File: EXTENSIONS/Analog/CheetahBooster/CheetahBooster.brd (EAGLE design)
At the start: 83 x 73 mm, 31 parts

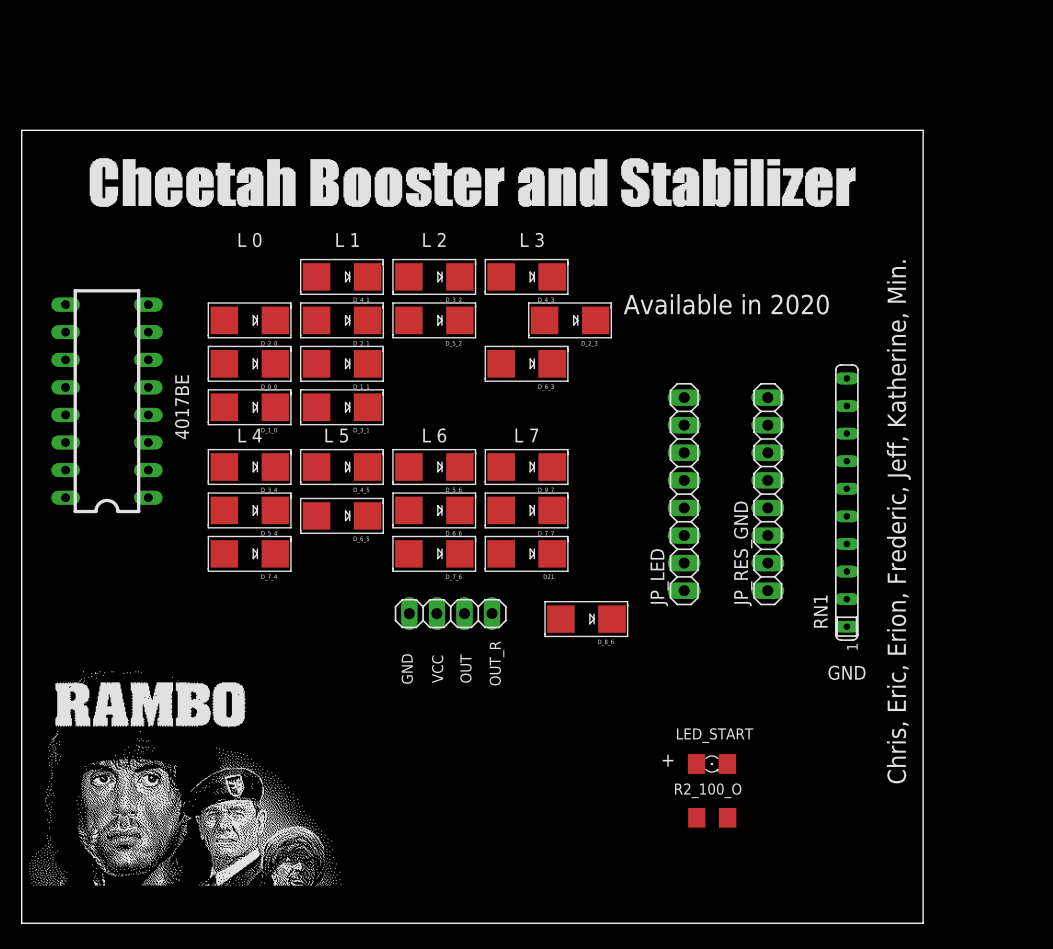
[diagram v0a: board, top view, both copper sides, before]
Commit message: Create CheetahBooster MCU
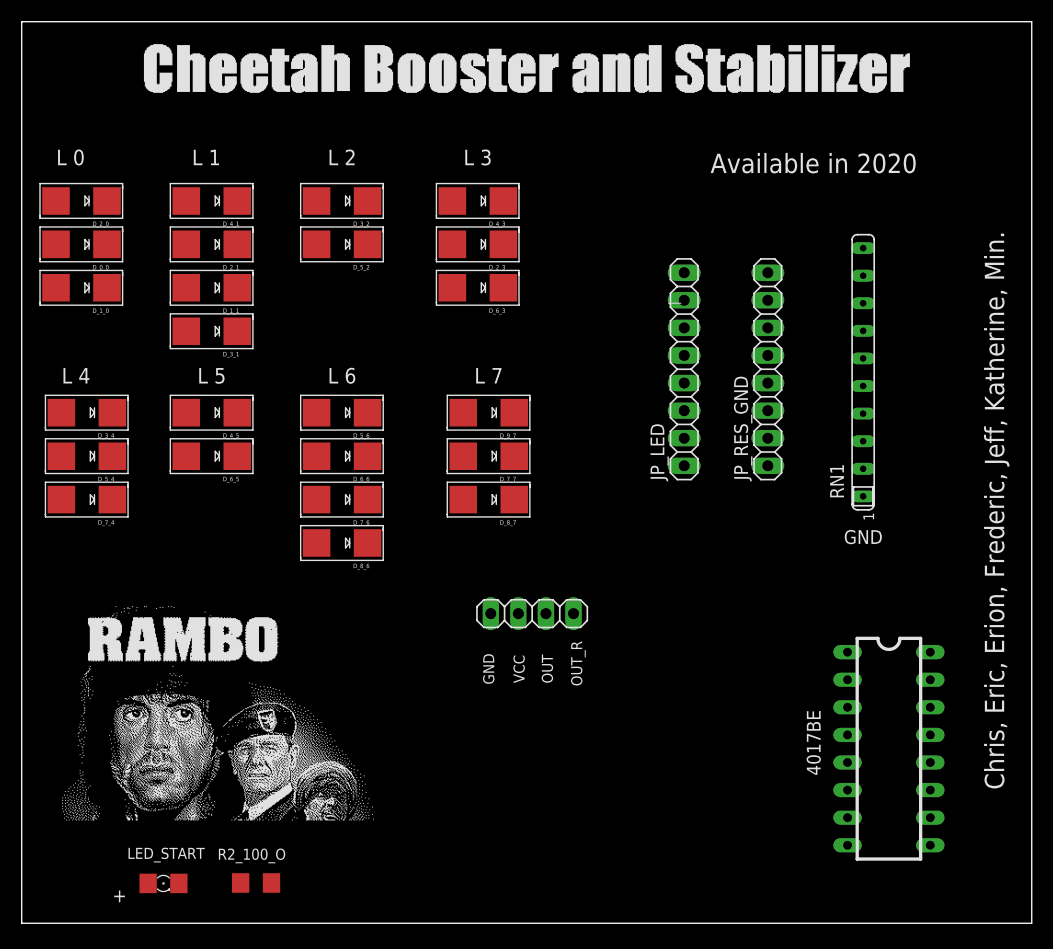
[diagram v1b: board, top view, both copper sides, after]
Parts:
- removed D21: (no value), adafruit:SMADIODE
- added D_8_7: (no value), adafruit:SMADIODE
- moved 4017BE 78.8 mm to (81.8, 28.1), turned to 270 degrees
- moved LED_START 51.7 mm to (15.1, 15.7)
- moved R2_100_O 42.4 mm to (23.6, 15.7)
- moved D_8_6 23.6 mm to (31.5, 47.0)
- moved D_0_0 19.0 mm to (7.50, 74.5)
- moved D_1_0 19.0 mm to (7.50, 70.5)
- moved D_2_0 19.0 mm to (7.50, 78.5)
- moved D_3_4 15.8 mm to (8.00, 59.0)
- moved D_5_4 15.8 mm to (8.00, 55.0)
- moved D_7_4 15.8 mm to (8.00, 51.0)
- moved D_1_1 13.9 mm to (19.5, 70.5)
- moved D_2_1 13.9 mm to (19.5, 74.5)
- moved D_3_1 13.9 mm to (19.5, 66.5)
- moved D_4_1 13.9 mm to (19.5, 78.5)
- moved D_6_5 13.2 mm to (19.5, 55.0)
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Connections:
- removed net D_8_7: D21.C
- removed net SEG_0_0: LED_START.A
- net LED_7: now also D_8_7.C
- net SEG_0: now also LED_START.A
- net SEG_8: now also D_8_7.A; no longer D21.A
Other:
- board size 83 x 73 mm -> 93 x 83 mm

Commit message: Create CheetahBooster MCU
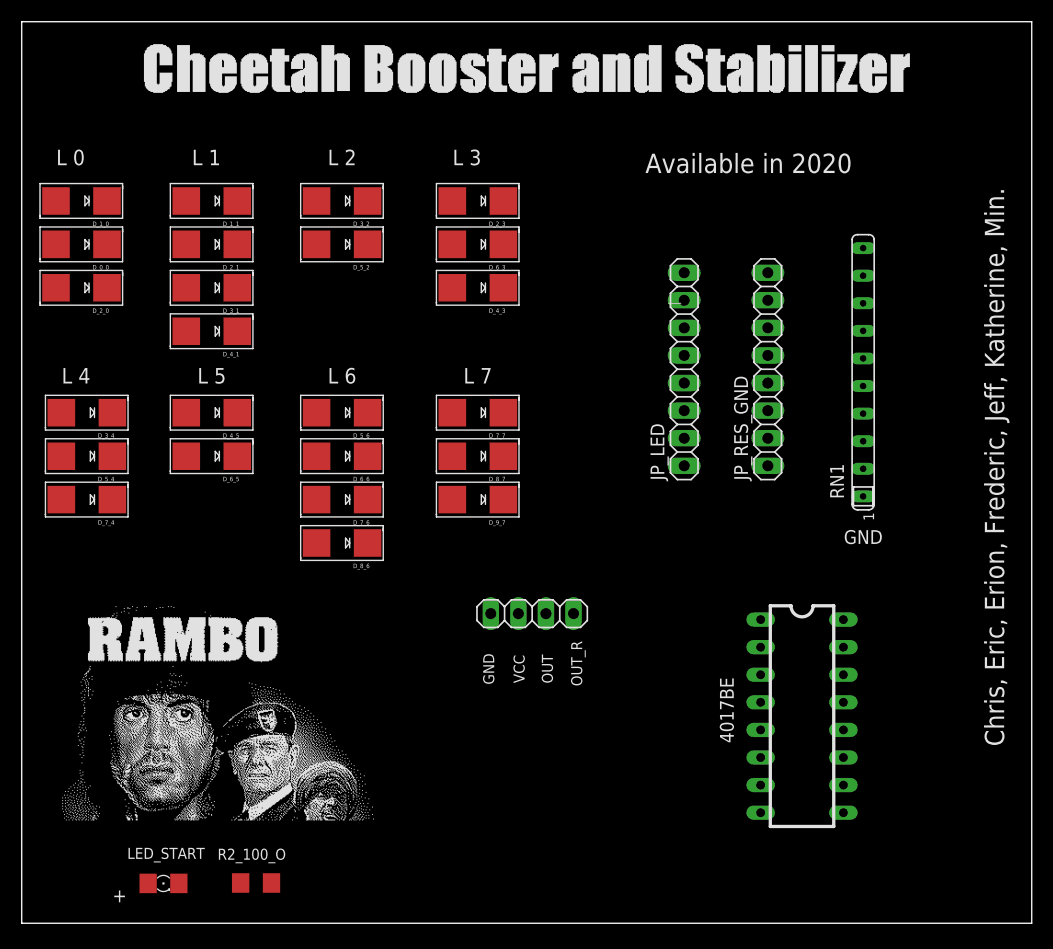
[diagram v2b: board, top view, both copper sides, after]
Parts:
- moved D_4_1 12.0 mm to (19.5, 66.5)
- moved 4017BE 8.54 mm to (73.8, 31.1)
- moved D_9_7 8.06 mm to (44.0, 51.0)
- moved D_1_0 8.00 mm to (7.50, 78.5)
- moved D_1_1 8.00 mm to (19.5, 78.5)
- moved D_2_0 8.00 mm to (7.50, 70.5)
- moved D_4_3 8.00 mm to (44.0, 70.5)
- moved D_7_7 4.12 mm to (44.0, 59.0)
- moved D_8_7 4.12 mm to (44.0, 55.0)
- moved D_2_3 4.00 mm to (44.0, 78.5)
- moved D_3_1 4.00 mm to (19.5, 70.5)
- moved D_6_3 4.00 mm to (44.0, 74.5)
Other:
- board text added: "CYCLE LED ================ 0 0 1 0, 1 2 0, 1, 3 3 1, 2, 4 4 1, 3, 5 5 2, 4, 6 6 3, 5, 6 7 4, 6, 7 8 6, 7 9 7"
- board text added: "PCBv2 - 2020.03"
- board text removed: "CYCLE/INSTRUCTION =============== LED 0 0,1,2,3 LED 1 1,2,4 LED 2 3,5 LED 3 2,4 LED 4 3,5,6 LED 5 4 LED 6 5,6,7 LED 7 6,7,8"
- board text removed: "PCBv1 - 2020.02"

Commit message: Create CheetahBooster MCU
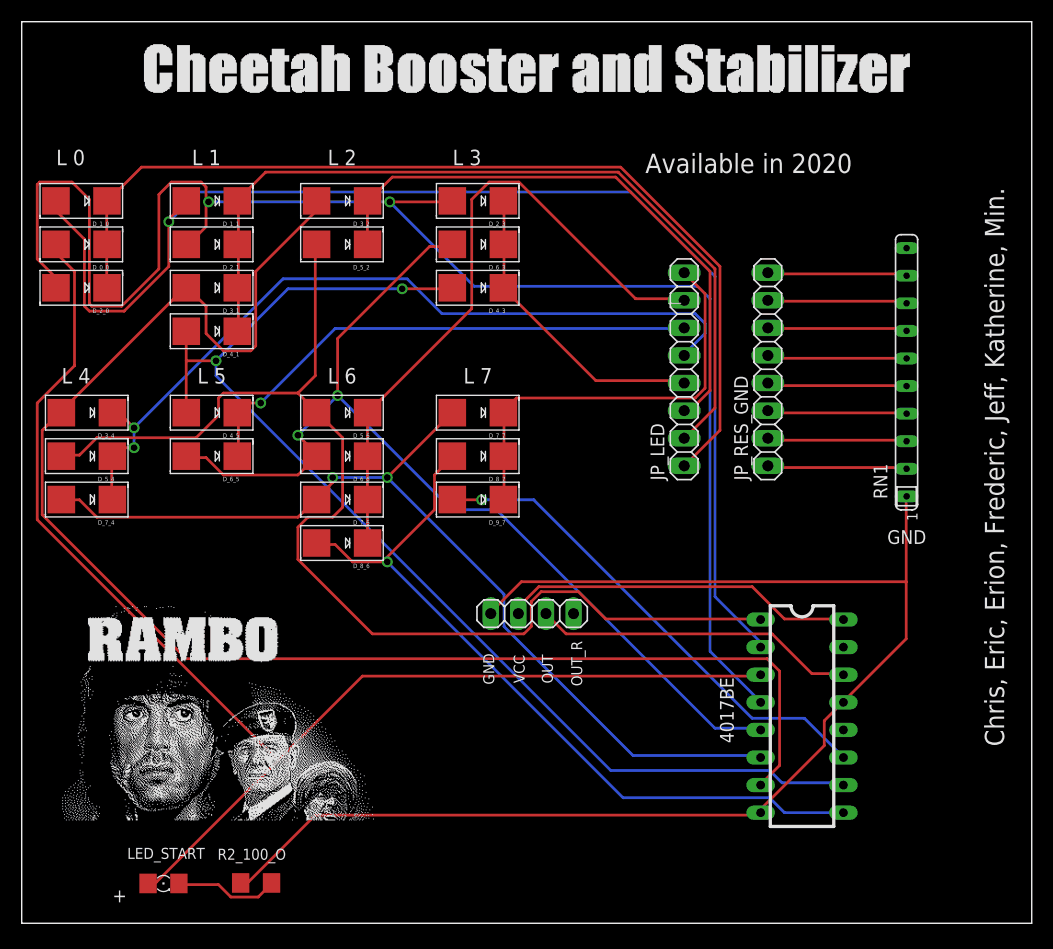
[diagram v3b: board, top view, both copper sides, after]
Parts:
- moved RN1 4.00 mm to (83.5, 62.8)
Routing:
- net SEG_2: track 0.00 -> 146.3 mm, vias 0 -> 2
- net SEG_3: track 0.00 -> 137.9 mm
- net GND: track 0.00 -> 124.9 mm
- net SEG_0: track 0.00 -> 123.2 mm
- net SEG_1: track 0.00 -> 117.7 mm, vias 0 -> 1
- net SEG_4: track 0.00 -> 109.6 mm, vias 0 -> 2
- net SEG_5: track 0.00 -> 109.1 mm
- net SEG_6: track 0.00 -> 92.5 mm, vias 0 -> 2
- net LED_0: track 0.00 -> 89.2 mm
- net SEG_7: track 0.00 -> 87.8 mm, vias 0 -> 2
- net LED_1: track 0.00 -> 77.9 mm
- net LED_4: track 0.00 -> 74.4 mm, vias 0 -> 2
- net SEG_8: track 0.00 -> 71.1 mm, vias 0 -> 1
- net LED_6: track 0.00 -> 60.4 mm
- net LED_2: track 0.00 -> 54.1 mm
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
